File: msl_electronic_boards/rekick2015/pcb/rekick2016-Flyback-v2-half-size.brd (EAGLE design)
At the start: 160 x 100 mm, 201 parts, among them IC1 74LVC1G02GW, IC2 4043D, IC3 LM1117, IC4 LM1458D, P1 39-30-06?_S, P2 39-30-08?_S, Q1 16MHz, Q2 IKW 25N120, Q3 PSMN7R8-120PS, Q5 IPD90P04P4L, Q6 IRF840, T1 BC859, T2 BC849, T3 BC849, T4 BC849, T5 IRLML6344TRPBF, T6 BC859, U1 TXB0108PWR, U3 LM2675, U4 LM2675, U5 ADUM4190BRIZ, U6 ADUM4190BRIZ, X1 87832-12, X2 87832-04

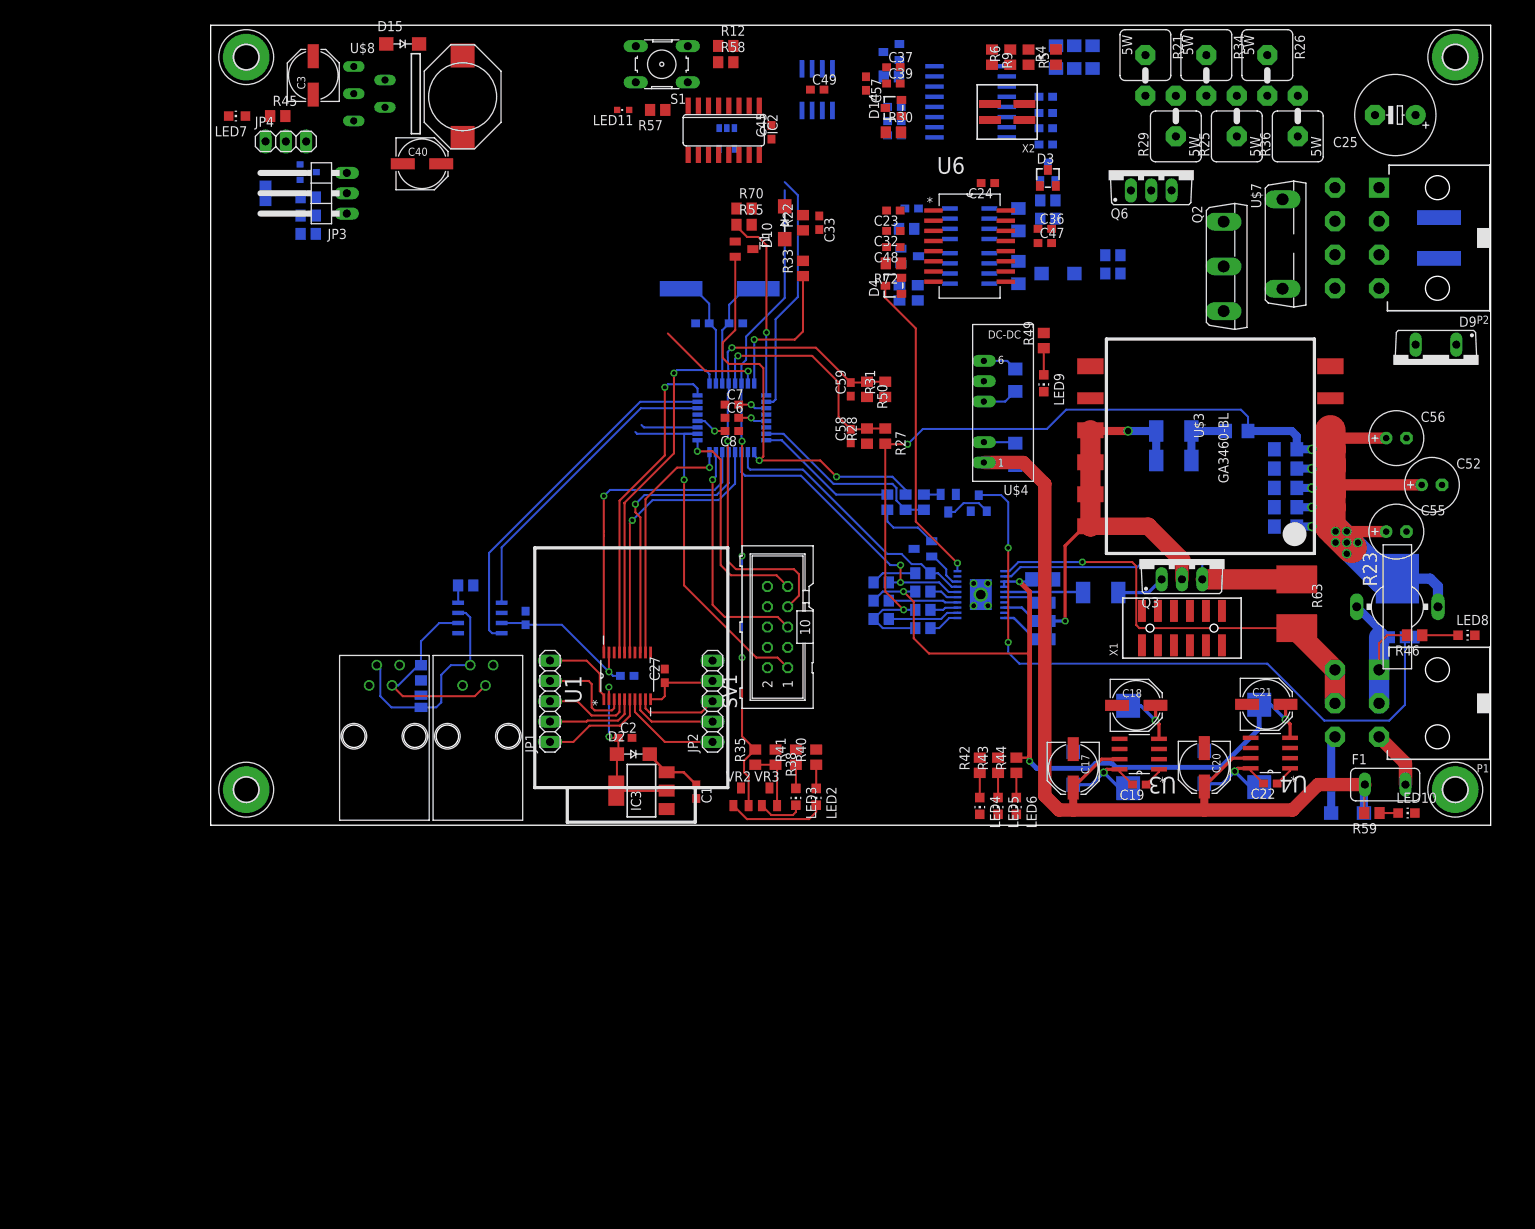
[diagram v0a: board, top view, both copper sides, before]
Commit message: rekick 2016 board for robocup workshop
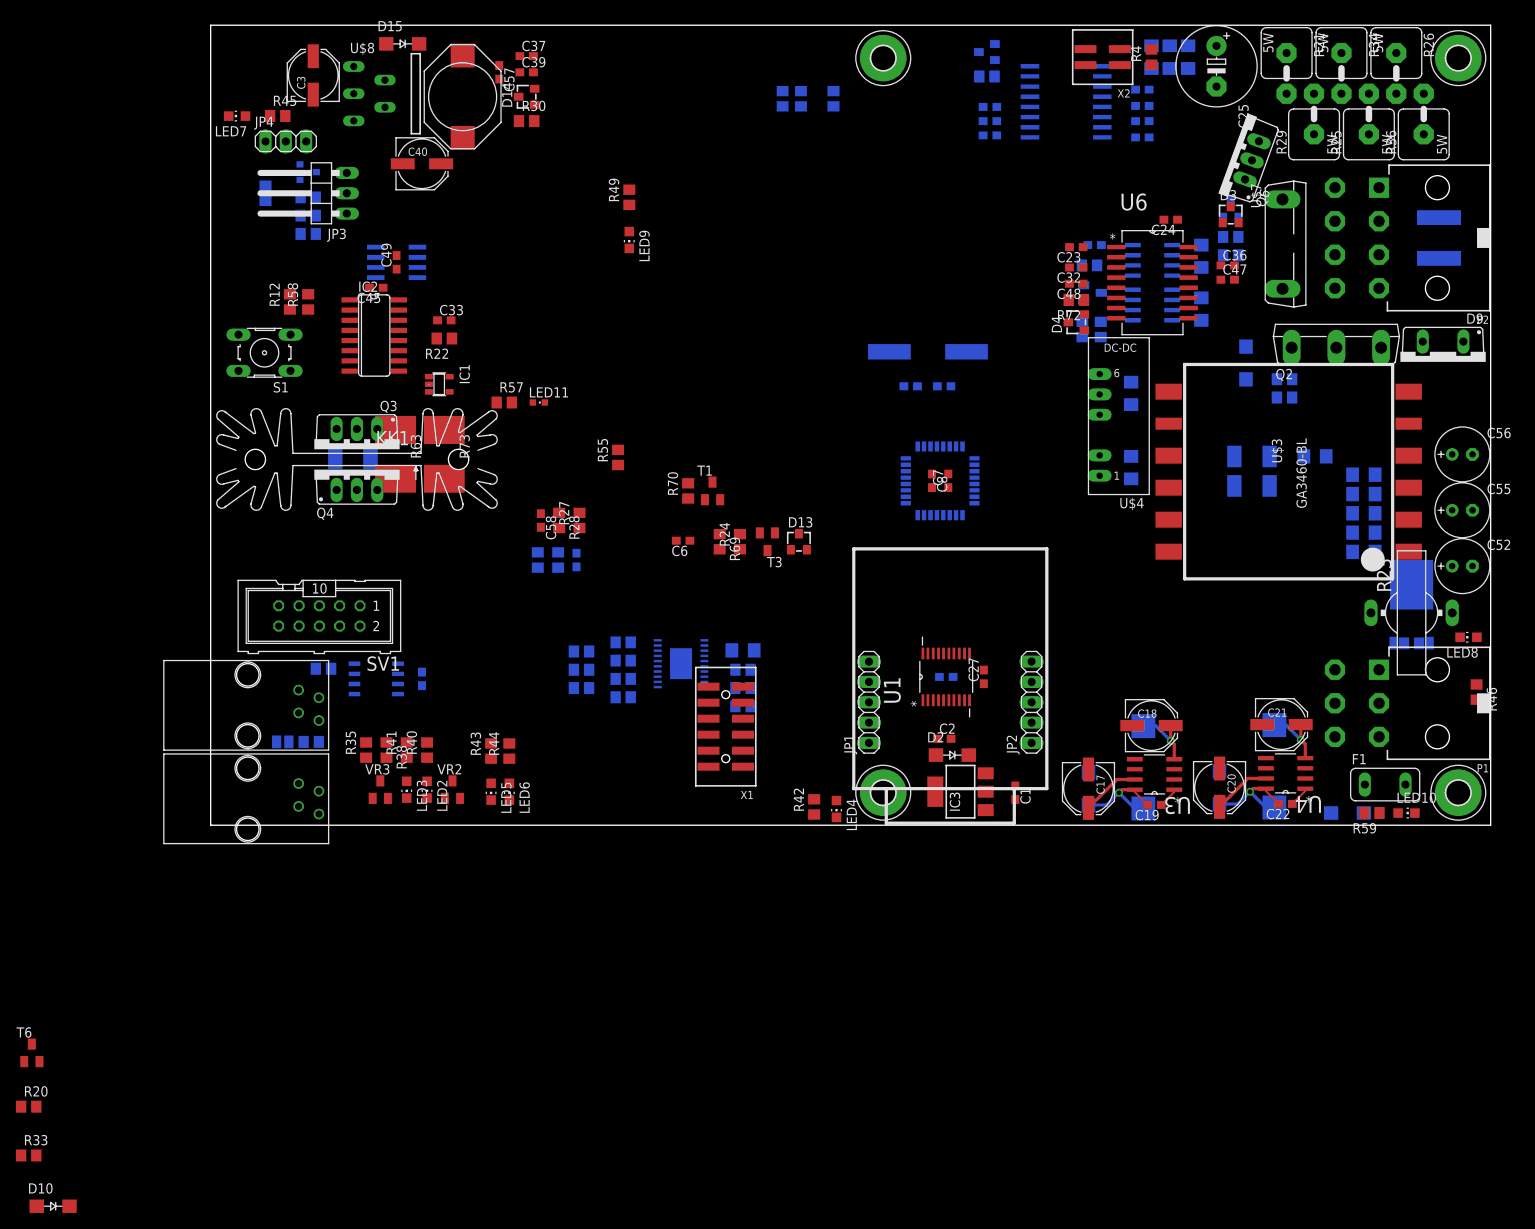
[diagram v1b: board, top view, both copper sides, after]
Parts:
- added KK1: SK104, heatsink:SK104
- added Q4: PSMN7R8-120PS, transistor-power:TO220BV
- added R73: 10m, R2818:R2818
- moved D10 153.2 mm to (-19.7, -47.6), turned to 0 degrees
- moved R33 147.2 mm to (-22.7, -41.3), turned to 0 degrees
- moved R20 131.3 mm to (-22.7, -35.2), flipped to the top, turned to 0 degrees
- moved T6 128.0 mm to (-22.4, -28.4), flipped to the top, turned to 0 degrees
- moved R63 114.2 mm to (23.1, 46.4)
- moved Q3 104.0 mm to (18.3, 47.0), turned to 180 degrees
- moved R66 95.0 mm to (17.8, 45.8), turned to 0 degrees
- moved H4 79.6 mm to (84.1, 4.06)
- moved H3 79.6 mm to (84.1, 95.9)
- moved LED5 63.4 mm to (35.1, 4.19)
- moved LED6 63.4 mm to (37.3, 4.19)
- moved R43 63.4 mm to (35.1, 9.27)
- moved R44 63.4 mm to (37.3, 9.27)
- moved R12 63.2 mm to (9.91, 65.4), turned to 90 degrees
- moved S1 61.4 mm to (6.73, 59.1)
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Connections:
- net +12V: no longer R30.2
- net +24V: now also R30.2
- net GND1: now also R73.P$2
- net N$17: now also Q4.S, R73.P$1
- net N$18: now also Q4.G
- net N$24: now also Q4.D
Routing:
- net 24V_BOOSTER: track 177.7 -> 0.00 mm, vias 13 -> 0
- net +24V: track 121.3 -> 14.5 mm
- net +12V: track 99.2 -> 8.50 mm, vias 4 -> 1
- net N$54: track 86.6 -> 0.00 mm, vias 2 -> 0
- net ADC_CAP: track 80.7 -> 0.00 mm, vias 3 -> 0
- net ADC_24V_LOGIK/SCK_A: track 62.2 -> 0.00 mm, vias 2 -> 0
- net N$24: track 57.3 -> 0.00 mm, vias 2 -> 0
- net CHARGE: track 57.3 -> 0.00 mm, vias 2 -> 0
- net GND1: track 56.2 -> 0.00 mm, vias 1 -> 0
- net OC0A/MOSI_A: track 45.7 -> 0.00 mm, vias 1 -> 0
- net CAN_RX: track 45.3 -> 0.00 mm
- net MOSI: track 43.5 -> 0.00 mm, vias 1 -> 0
- net MISO: track 40.8 -> 0.00 mm, vias 1 -> 0
- net +5V: track 49.5 -> 8.77 mm, vias 4 -> 1
- net N$17: track 39.6 -> 0.00 mm
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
